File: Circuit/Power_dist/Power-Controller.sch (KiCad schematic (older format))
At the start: 41 parts, among them P15 USB_B, U1 93LC56BT-I/OT, U2 FT232H, U3 ACPL-247-500E, U4 ACPL-247-500E, Y1 12MHz

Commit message: edit sch and add pcix16
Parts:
- P15: footprint Connect:USB_Mini-B -> Connectors:USB_Mini-B
- U3, U4: footprint Zeabus:SO16_4.4x10.3mm_Pitch1.27mm -> zeabus:SO16_4.4x10.3mm_Pitch1.27mm
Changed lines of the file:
@@
 EESchema Schematic File Version 2
+LIBS:Power_Distributor-rescue
 LIBS:power
 LIBS:device
@@
 LIBS:zeabus
 LIBS:ftdi
+LIBS:Power_Distributor-cache
 EELAYER 25 0
 EELAYER END
@@
 F 0 "P15" V 1650 3450 50  0000 C CNN
 F 1 "USB_B" H 1950 3700 50  0000 C CNN
-F 2 "Connect:USB_Mini-B" V 1900 3250 60  0001 C CNN
+F 2 "Connectors:USB_Mini-B" V 1900 3250 60  0001 C CNN
 F 3 "" V 1900 3250 60  0000 C CNN
 	1    1950 3350
@@
 	5000 3550 4650 3550
 $Comp
-L +3.3V #PWR016
+L +3.3V #PWR039
 U 1 1 58C66432
 P 4050 3700
-F 0 "#PWR016" H 4050 3550 50  0001 C CNN
+F 0 "#PWR039" H 4050 3550 50  0001 C CNN
 F 1 "+3.3V" H 4050 3840 50  0000 C CNN
 F 2 "" H 4050 3700 50  0000 C CNN
@@
 $EndComp
 $Comp
-L +3.3V #PWR017
+L +3.3V #PWR040
 U 1 1 58C66491
 P 2200 4300
-F 0 "#PWR017" H 2200 4150 50  0001 C CNN
+F 0 "#PWR040" H 2200 4150 50  0001 C CNN
 F 1 "+3.3V" H 2200 4440 50  0000 C CNN
 F 2 "" H 2200 4300 50  0000 C CNN
@@
 Connection ~ 3650 2650
 $Comp
-L VBUS #PWR018
+L VBUS #PWR041
 U 1 1 58C68317
 P 3650 2550
-F 0 "#PWR018" H 3650 2510 30  0001 C CNN
+F 0 "#PWR041" H 3650 2510 30  0001 C CNN
 F 1 "VBUS" H 3650 2660 30  0000 C CNN
 F 2 "" H 3650 2550 60  0000 C CNN
@@
 Connection ~ 5350 1750
 $Comp
-L +3.3V #PWR019
+L +3.3V #PWR042
 U 1 1 58C6B629
 P 4150 1700
-F 0 "#PWR019" H 4150 1550 50  0001 C CNN
+F 0 "#PWR042" H 4150 1550 50  0001 C CNN
 F 1 "+3.3V" H 4150 1840 50  0000 C CNN
 F 2 "" H 4150 1700 50  0000 C CNN
@@
 Connection ~ 6150 2350
 $Comp
-L +3.3V #PWR020
+L +3.3V #PWR043
 U 1 1 58C6D78F
 P 6400 2300
-F 0 "#PWR020" H 6400 2150 50  0001 C CNN
+F 0 "#PWR043" H 6400 2150 50  0001 C CNN
 F 1 "+3.3V" H 6400 2440 50  0000 C CNN
 F 2 "" H 6400 2300 50  0000 C CNN
@@
 F 0 "U4" H 8700 4450 50  0000 L CNN
 F 1 "ACPL-247-500E" H 8600 4050 50  0000 L CNN
-F 2 "Zeabus:SO16_4.4x10.3mm_Pitch1.27mm" H 8900 4250 50  0001 L CNN
+F 2 "zeabus:SO16_4.4x10.3mm_Pitch1.27mm" H 8900 4250 50  0001 L CNN
 F 3 "" H 8900 4250 50  0000 L CNN
 	1    8900 4250
@@
 F 0 "U4" H 8700 5050 50  0000 L CNN
 F 1 "ACPL-247-500E" H 8600 4650 50  0000 L CNN
-F 2 "Zeabus:SO16_4.4x10.3mm_Pitch1.27mm" H 8900 4850 50  0001 L CNN
+F 2 "zeabus:SO16_4.4x10.3mm_Pitch1.27mm" H 8900 4850 50  0001 L CNN
 F 3 "" H 8900 4850 50  0000 L CNN
 	2    8900 4850
@@
 F 0 "U4" H 8700 5650 50  0000 L CNN
 F 1 "ACPL-247-500E" H 8600 5250 50  0000 L CNN
-F 2 "Zeabus:SO16_4.4x10.3mm_Pitch1.27mm" H 8900 5450 50  0001 L CNN
+F 2 "zeabus:SO16_4.4x10.3mm_Pitch1.27mm" H 8900 5450 50  0001 L CNN
 F 3 "" H 8900 5450 50  0000 L CNN
 	3    8900 5450
@@
 F 0 "U4" H 8700 6250 50  0000 L CNN
 F 1 "ACPL-247-500E" H 8600 5850 50  0000 L CNN
-F 2 "Zeabus:SO16_4.4x10.3mm_Pitch1.27mm" H 8900 6050 50  0001 L CNN
+F 2 "zeabus:SO16_4.4x10.3mm_Pitch1.27mm" H 8900 6050 50  0001 L CNN
 F 3 "" H 8900 6050 50  0000 L CNN
 	4    8900 6050
@@
 F 0 "U3" H 8700 2050 50  0000 L CNN
 F 1 "ACPL-247-500E" H 8600 1650 50  0000 L CNN
-F 2 "Zeabus:SO16_4.4x10.3mm_Pitch1.27mm" H 8900 1850 50  0001 L CNN
+F 2 "zeabus:SO16_4.4x10.3mm_Pitch1.27mm" H 8900 1850 50  0001 L CNN
 F 3 "" H 8900 1850 50  0000 L CNN
 	1    8900 1850
@@
 F 0 "U3" H 8700 2650 50  0000 L CNN
 F 1 "ACPL-247-500E" H 8600 2250 50  0000 L CNN
-F 2 "Zeabus:SO16_4.4x10.3mm_Pitch1.27mm" H 8900 2450 50  0001 L CNN
+F 2 "zeabus:SO16_4.4x10.3mm_Pitch1.27mm" H 8900 2450 50  0001 L CNN
 F 3 "" H 8900 2450 50  0000 L CNN
 	2    8900 2450
@@
 F 0 "U3" H 8700 3250 50  0000 L CNN
 F 1 "ACPL-247-500E" H 8600 2850 50  0000 L CNN
-F 2 "Zeabus:SO16_4.4x10.3mm_Pitch1.27mm" H 8900 3050 50  0001 L CNN
+F 2 "zeabus:SO16_4.4x10.3mm_Pitch1.27mm" H 8900 3050 50  0001 L CNN
 F 3 "" H 8900 3050 50  0000 L CNN
 	3    8900 3050
@@
 F 0 "U3" H 8700 3850 50  0000 L CNN
 F 1 "ACPL-247-500E" H 8600 3450 50  0000 L CNN
-F 2 "Zeabus:SO16_4.4x10.3mm_Pitch1.27mm" H 8900 3650 50  0001 L CNN
+F 2 "zeabus:SO16_4.4x10.3mm_Pitch1.27mm" H 8900 3650 50  0001 L CNN
 F 3 "" H 8900 3650 50  0000 L CNN
 	4    8900 3650
@@
 Connection ~ 1850 2900
 $Comp
-L GNDD #PWR021
+L GNDD #PWR044
 U 1 1 58F494A1
 P 8550 2050
-F 0 "#PWR021" H 8550 1800 50  0001 C CNN
+F 0 "#PWR044" H 8550 1800 50  0001 C CNN
 F 1 "GNDD" H 8550 1900 50  0000 C CNN
 F 2 "" H 8550 2050 50  0001 C CNN
@@
 $EndComp
 $Comp
-L GNDD #PWR022
+L GNDD #PWR045
 U 1 1 58F498ED
 P 1450 2950
-F 0 "#PWR022" H 1450 2700 50  0001 C CNN
+F 0 "#PWR045" H 1450 2700 50  0001 C CNN
 F 1 "GNDD" H 1450 2800 50  0000 C CNN
 F 2 "" H 1450 2950 50  0001 C CNN
@@
 $EndComp
 $Comp
-L GNDD #PWR023
+L GNDD #PWR046
 U 1 1 58F499B5
 P 3250 2950
-F 0 "#PWR023" H 3250 2700 50  0001 C CNN
+F 0 "#PWR046" H 3250 2700 50  0001 C CNN
 F 1 "GNDD" H 3250 2800 50  0000 C CNN
 F 2 "" H 3250 2950 50  0001 C CNN
@@
 $EndComp
 $Comp
-L GNDD #PWR024
+L GNDD #PWR047
 U 1 1 58F49A7D
 P 4150 2050
-F 0 "#PWR024" H 4150 1800 50  0001 C CNN
+F 0 "#PWR047" H 4150 1800 50  0001 C CNN
 F 1 "GNDD" H 4150 1900 50  0000 C CNN
 F 2 "" H 4150 2050 50  0001 C CNN
@@
 $EndComp
 $Comp
-L GNDD #PWR025
+L GNDD #PWR048
 U 1 1 58F49B45
 P 5350 2050
-F 0 "#PWR025" H 5350 1800 50  0001 C CNN
+F 0 "#PWR048" H 5350 1800 50  0001 C CNN
 F 1 "GNDD" H 5350 1900 50  0000 C CNN
 F 2 "" H 5350 2050 50  0001 C CNN
@@
 $EndComp
 $Comp
-L GNDD #PWR026
+L GNDD #PWR049
 U 1 1 58F49C0D
 P 5350 2550
-F 0 "#PWR026" H 5350 2300 50  0001 C CNN
+F 0 "#PWR049" H 5350 2300 50  0001 C CNN
 F 1 "GNDD" H 5350 2400 50  0000 C CNN
 F 2 "" H 5350 2550 50  0001 C CNN
@@
 $EndComp
 $Comp
-L GNDD #PWR027
+L GNDD #PWR050
 U 1 1 58F49CD5
 P 6400 2700
-F 0 "#PWR027" H 6400 2450 50  0001 C CNN
+F 0 "#PWR050" H 6400 2450 50  0001 C CNN
 F 1 "GNDD" H 6400 2550 50  0000 C CNN
 F 2 "" H 6400 2700 50  0001 C CNN
@@
 $EndComp
 $Comp
-L GNDD #PWR028
+L GNDD #PWR051
 U 1 1 58F49D9D
 P 4450 3550
-F 0 "#PWR028" H 4450 3300 50  0001 C CNN
+F 0 "#PWR051" H 4450 3300 50  0001 C CNN
 F 1 "GNDD" H 4450 3400 50  0000 C CNN
 F 2 "" H 4450 3550 50  0001 C CNN
@@
 $EndComp
 $Comp
-L GNDD #PWR029
+L GNDD #PWR052
 U 1 1 58F4A0C7
 P 2200 5150
-F 0 "#PWR029" H 2200 4900 50  0001 C CNN
+F 0 "#PWR052" H 2200 4900 50  0001 C CNN
 F 1 "GNDD" H 2200 5000 50  0000 C CNN
 F 2 "" H 2200 5150 50  0001 C CNN
@@
 $EndComp
 $Comp
-L GNDD #PWR030
+L GNDD #PWR053
 U 1 1 58F4A4EB
 P 4050 4250
-F 0 "#PWR030" H 4050 4000 50  0001 C CNN
+F 0 "#PWR053" H 4050 4000 50  0001 C CNN
 F 1 "GNDD" H 4050 4100 50  0000 C CNN
 F 2 "" H 4050 4250 50  0001 C CNN
@@
 $EndComp
 $Comp
-L GNDD #PWR031
+L GNDD #PWR054
 U 1 1 58F4A583
 P 4500 4250
-F 0 "#PWR031" H 4500 4000 50  0001 C CNN
+F 0 "#PWR054" H 4500 4000 50  0001 C CNN
 F 1 "GNDD" H 4500 4100 50  0000 C CNN
 F 2 "" H 4500 4250 50  0001 C CNN
@@
 $EndComp
 $Comp
-L GNDD #PWR032
+L GNDD #PWR055
 U 1 1 58F4A765
 P 5350 6300
-F 0 "#PWR032" H 5350 6050 50  0001 C CNN
+F 0 "#PWR055" H 5350 6050 50  0001 C CNN
 F 1 "GNDD" H 5350 6150 50  0000 C CNN
 F 2 "" H 5350 6300 50  0001 C CNN
@@
 $EndComp
 $Comp
-L GNDD #PWR033
+L GNDD #PWR056
 U 1 1 58F4B319
 P 8550 2650
-F 0 "#PWR033" H 8550 2400 50  0001 C CNN
+F 0 "#PWR056" H 8550 2400 50  0001 C CNN
 F 1 "GNDD" H 8550 2500 50  0000 C CNN
 F 2 "" H 8550 2650 50  0001 C CNN
@@
 $EndComp
 $Comp
-L GNDD #PWR034
+L GNDD #PWR057
 U 1 1 58F4B3B1
 P 8550 3250
-F 0 "#PWR034" H 8550 3000 50  0001 C CNN
+F 0 "#PWR057" H 8550 3000 50  0001 C CNN
 F 1 "GNDD" H 8550 3100 50  0000 C CNN
 F 2 "" H 8550 3250 50  0001 C CNN
@@
 $EndComp
 $Comp
-L GNDD #PWR035
+L GNDD #PWR058
 U 1 1 58F4B449
 P 8550 3850
-F 0 "#PWR035" H 8550 3600 50  0001 C CNN
+F 0 "#PWR058" H 8550 3600 50  0001 C CNN
 F 1 "GNDD" H 8550 3700 50  0000 C CNN
 F 2 "" H 8550 3850 50  0001 C CNN
@@
 $EndComp
 $Comp
-L GNDD #PWR036
+L GNDD #PWR059
 U 1 1 58F4B804
 P 8550 4450
-F 0 "#PWR036" H 8550 4200 50  0001 C CNN
+F 0 "#PWR059" H 8550 4200 50  0001 C CNN
 F 1 "GNDD" H 8550 4300 50  0000 C CNN
 F 2 "" H 8550 4450 50  0001 C CNN
@@
 $EndComp
 $Comp
-L GNDD #PWR037
+L GNDD #PWR060
 U 1 1 58F4B89C
 P 8550 5050
-F 0 "#PWR037" H 8550 4800 50  0001 C CNN
+F 0 "#PWR060" H 8550 4800 50  0001 C CNN
 F 1 "GNDD" H 8550 4900 50  0000 C CNN
 F 2 "" H 8550 5050 50  0001 C CNN
@@
 $EndComp
 $Comp
-L GNDD #PWR038
+L GNDD #PWR061
 U 1 1 58F4B934
 P 8550 5650
-F 0 "#PWR038" H 8550 5400 50  0001 C CNN
+F 0 "#PWR061" H 8550 5400 50  0001 C CNN
 F 1 "GNDD" H 8550 5500 50  0000 C CNN
 F 2 "" H 8550 5650 50  0001 C CNN
@@
 $EndComp
 $Comp
-L GNDD #PWR039
+L GNDD #PWR062
 U 1 1 58F4B9CC
 P 8550 6250
-F 0 "#PWR039" H 8550 6000 50  0001 C CNN
+F 0 "#PWR062" H 8550 6000 50  0001 C CNN
 F 1 "GNDD" H 8550 6100 50  0000 C CNN
 F 2 "" H 8550 6250 50  0001 C CNN

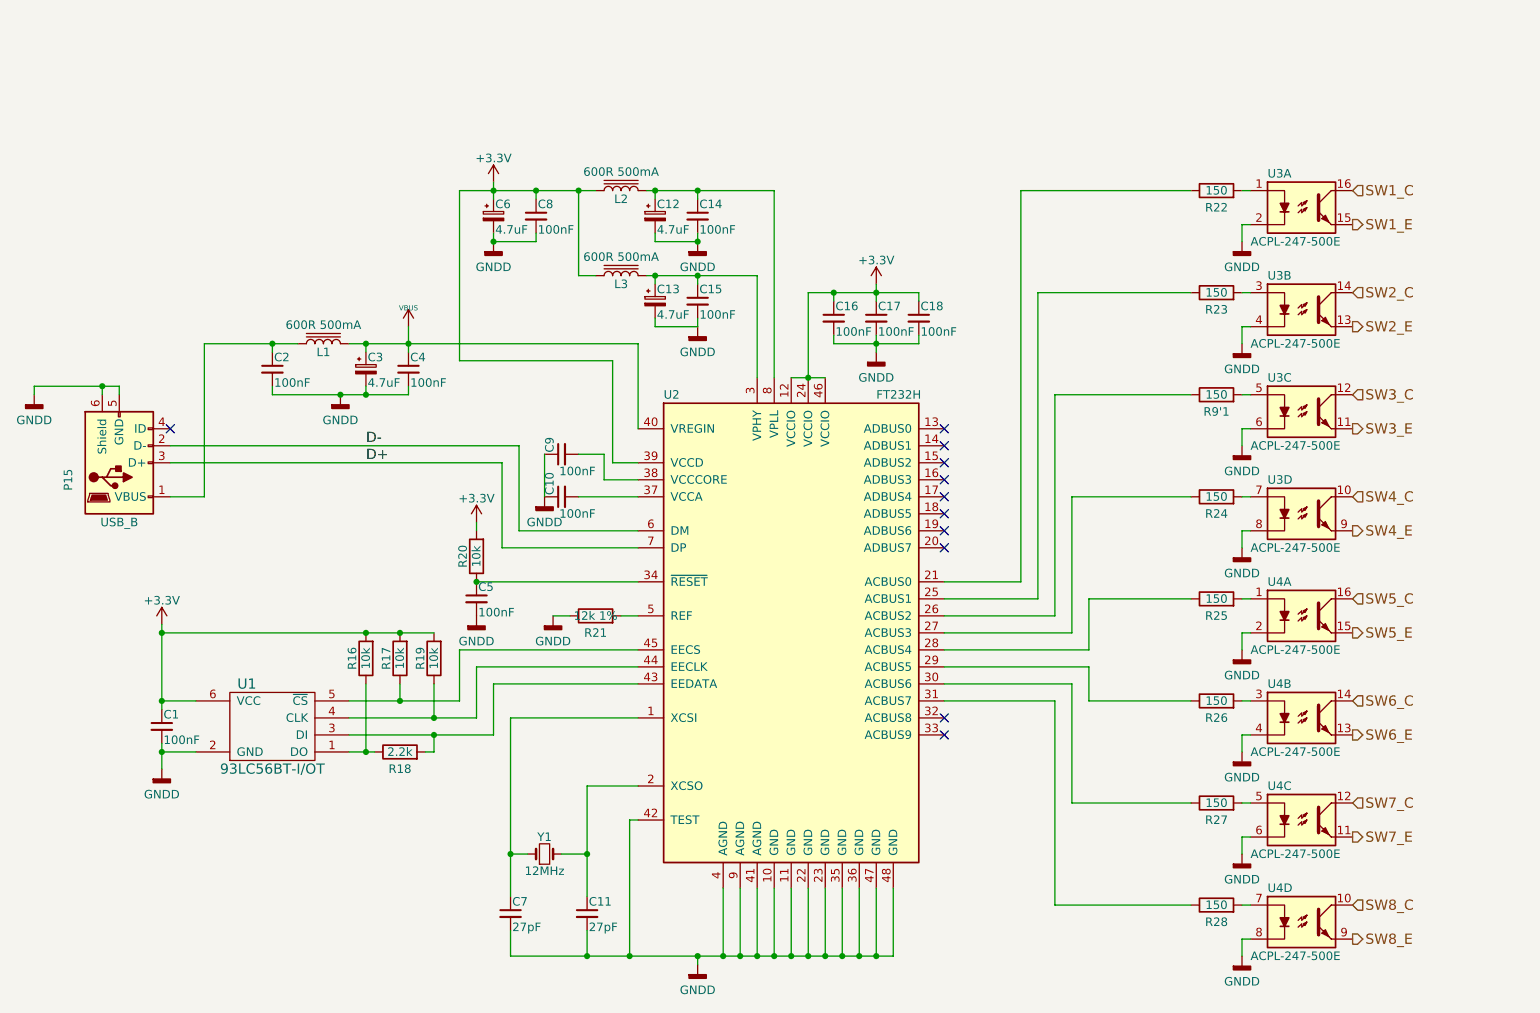
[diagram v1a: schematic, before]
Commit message: delete fuses at thrusters and oring + add power on jumper
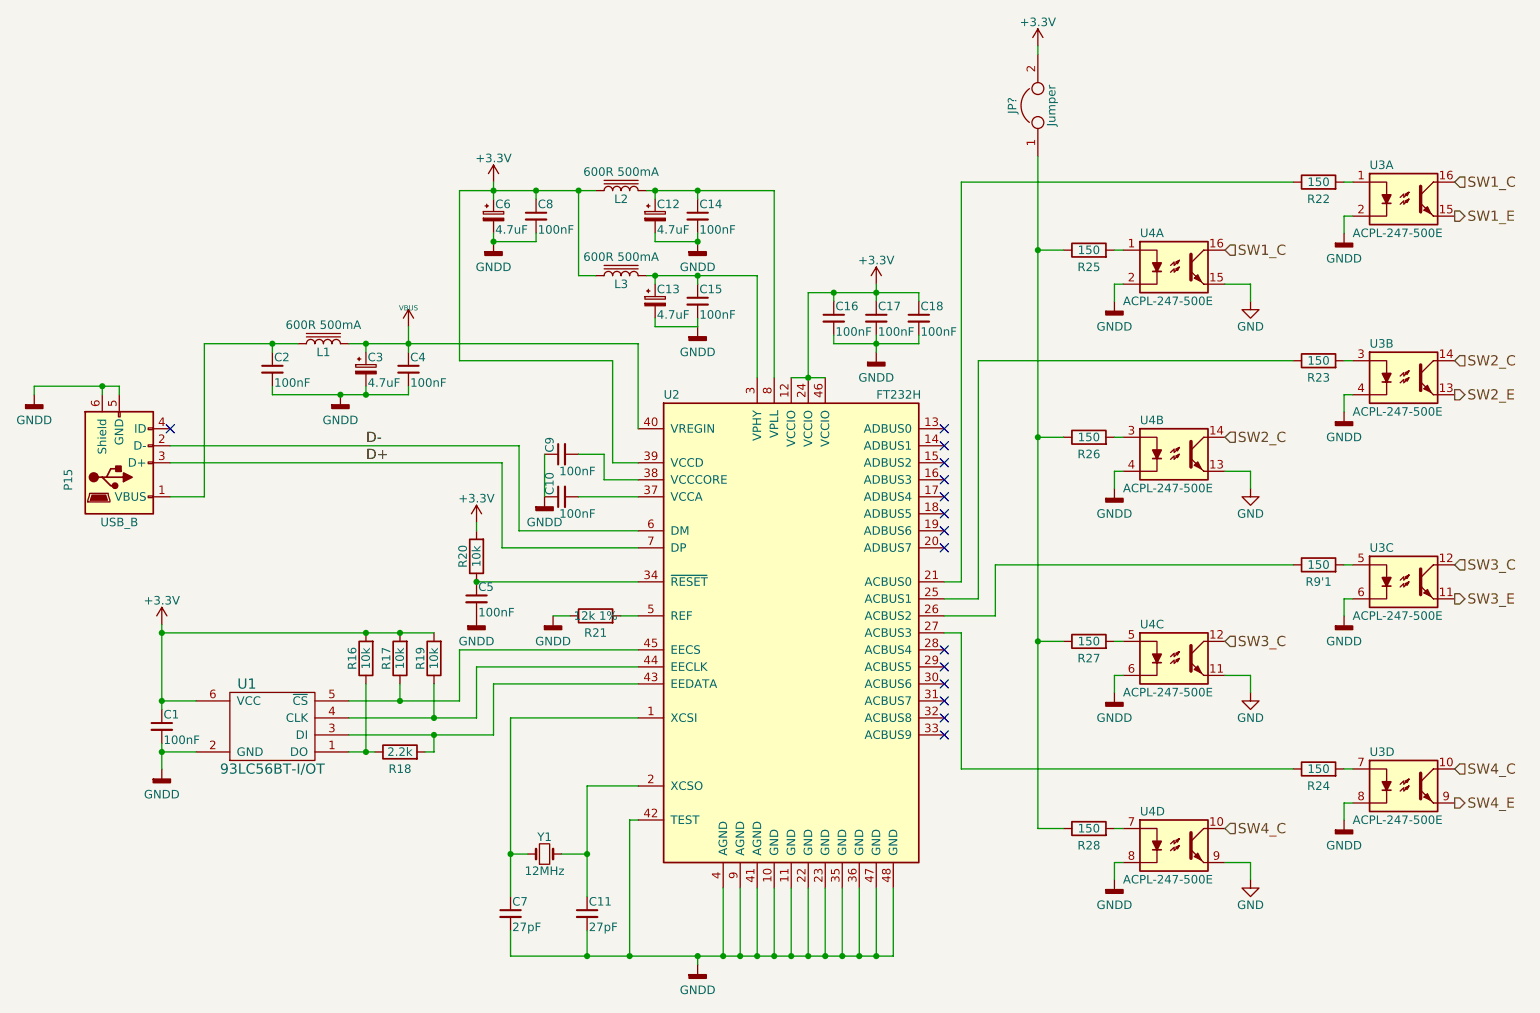
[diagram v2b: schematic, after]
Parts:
- added JP?: Jumper, Pin_Headers:Pin_Header_Straight_1x02_Pitch2.54mm, symbol Jumper
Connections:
- net SW5_C is gone; now on net SW1_C: U4.16
- net SW6_C is gone; now on net SW2_C: U4.14
- net SW6_E is gone; now on net GND: U4.13
- net SW7_C is gone; now on net SW3_C: U4.12
- net SW7_E is gone; now on net GND: U4.11
- net SW8_C is gone; now on net SW4_C: U4.10
- net SW8_E is gone; now on net GND: U4.9
- net +3V3: now also JP?.2
- net at U2.28 (ACBUS4): no longer R25.1
- net at U2.29 (ACBUS5): no longer R26.1
- net at U2.30 (ACBUS6): no longer R27.1
- net at U2.31 (ACBUS7): no longer R28.1
- net SW5_E renamed GND
- new net: JP?.1, R25.1, R26.1, R27.1, R28.1
- no-connect marks 11 -> 15
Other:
- moved on the sheet: R22, R23, R24, R25, R26, R27, R28, R9'1, U3A, U3B, U3C, U3D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

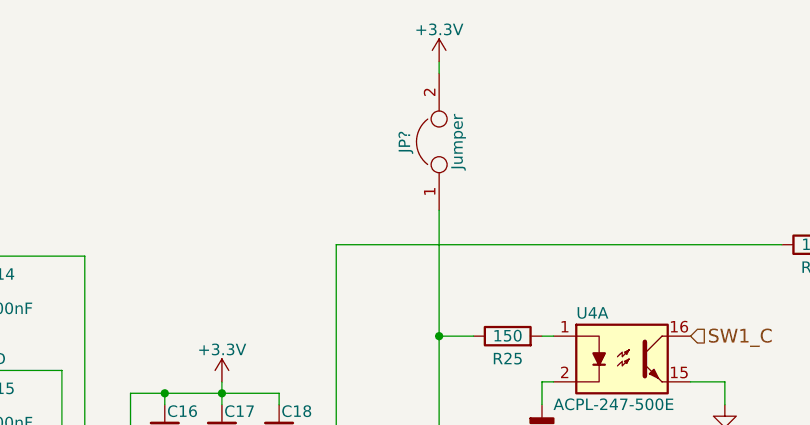
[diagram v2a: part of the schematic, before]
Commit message: component alignment on pcb
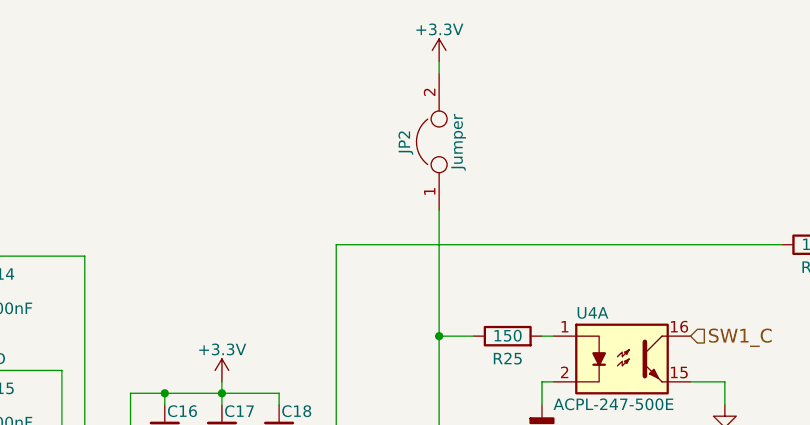
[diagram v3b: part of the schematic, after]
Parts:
- C1, C10, C11, C14, C15, C16, C17, C18, C2, C4, C5, C7, C8, C9, L1, L2, L3: footprint Capacitors_SMD:C_0603 -> Capacitors_SMD:C_0603_HandSoldering
- C12, C13, C3, C6: footprint Capacitors_SMD:C_0805 -> Capacitors_SMD:C_0805_HandSoldering
- R16, R17, R18, R19, R20, R21, R22, R23, R24, R25, R26, R27, R28, R9'1: footprint Resistors_SMD:R_0603 -> Resistors_SMD:R_0603_HandSoldering
- gave numbers to parts that had none: 1

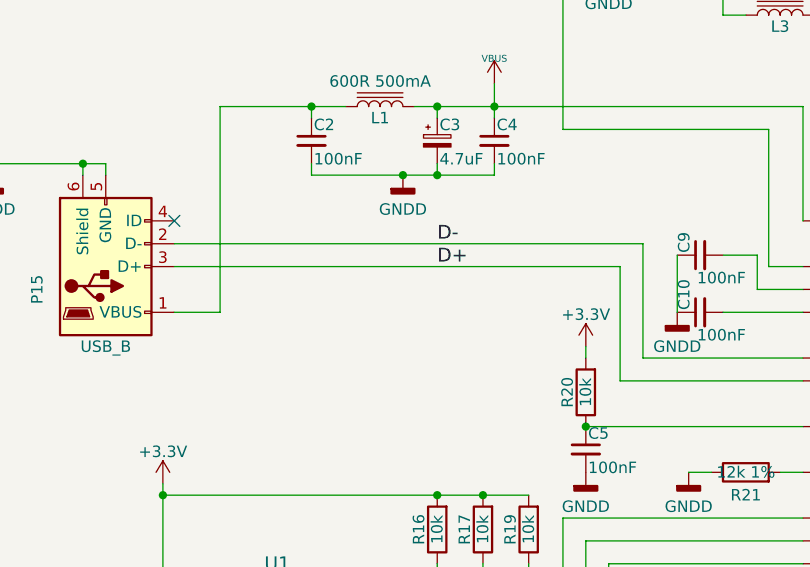
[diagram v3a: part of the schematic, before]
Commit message: fix USB_B Conn too far from edge
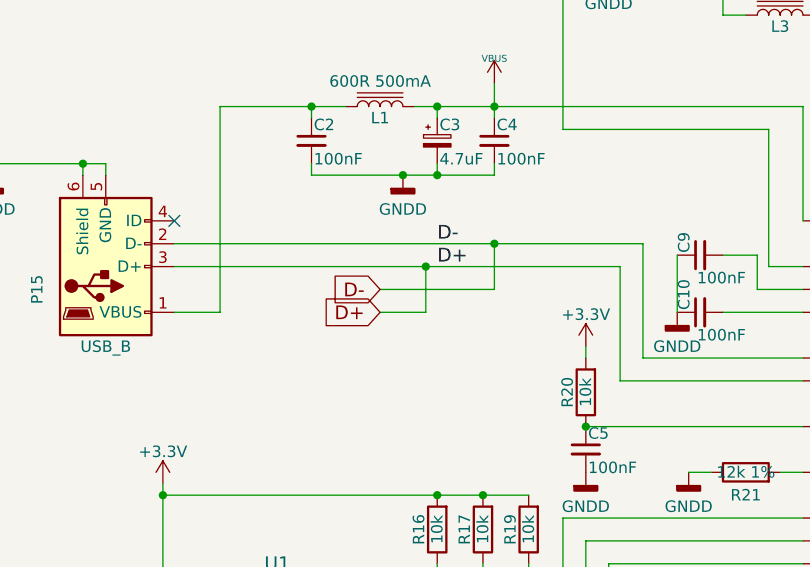
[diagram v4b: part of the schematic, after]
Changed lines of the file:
@@
 NoConn ~ 6800 4650
 NoConn ~ 6800 4750
+Wire Wire Line
+	3350 3350 3350 3550
+Wire Wire Line
+	3350 3550 3150 3550
+Connection ~ 3350 3350
+Wire Wire Line
+	3650 3250 3650 3450
+Wire Wire Line
+	3650 3450 3150 3450
+Connection ~ 3650 3250
+Text GLabel 3150 3450 0    60   Input ~ 0
+D-
+Text GLabel 3150 3550 0    60   Input ~ 0
+D+
 $EndSCHEMATC
